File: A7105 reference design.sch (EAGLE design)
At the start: 38 parts, among them J1 JST-SH-3, SW1 BUTTON, U1 A7105, U2 ATTINY167, U3 NMOS, X1 ECX-2236

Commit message: Finished integrated rev 0.2
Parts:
- removed J1: JST-SH-3, nikdavis:JST-SH-3
- removed U$3, U$4: TESTPAD, AlienWhoop:TESTPAD
- added C19: 1uF, Perfect_0402:CAP_0402
- added U$10, U$11, U$12, U$6, U$7, U$8, U$9: TESTPAD, AlienWhoop:TESTPAD
- U3: value NMOS -> NMOSSOT833B/1006; device nikdavis:NMOS -> nikdavis:NMOSSOT833B/1006
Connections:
- new net GPIO1: U1.GIO1, U2.PA0
- net GND: now also C19.2, U$9.1; no longer J1.2, J1.P$1, U$4.1
- net MOSI: now also U$12.1
- net RESET: now also U$7.1
- net SBUS: now also U$6.1; no longer J1.3
- net SCK: now also U$10.1
- net SDIO: now also U$11.1
- net VCC: now also C19.1, U$8.1; no longer J1.1, U$3.1

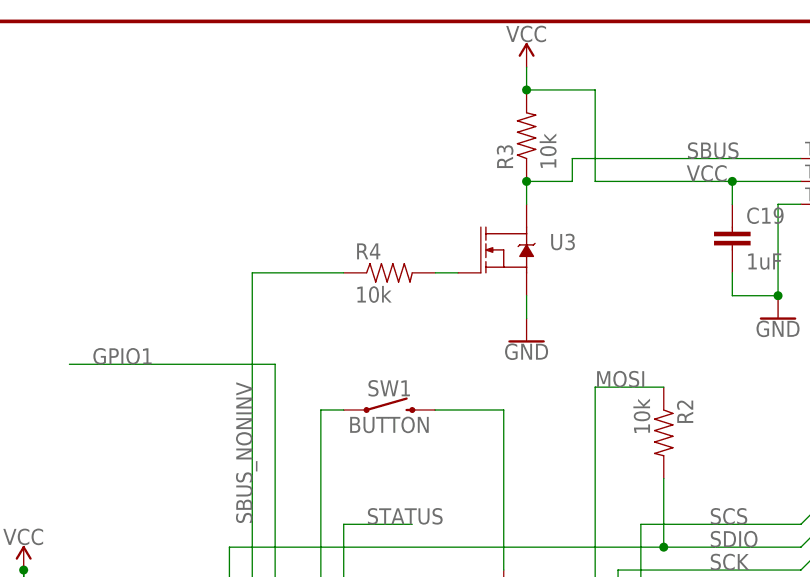
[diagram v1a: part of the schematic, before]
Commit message: Add bind pull up
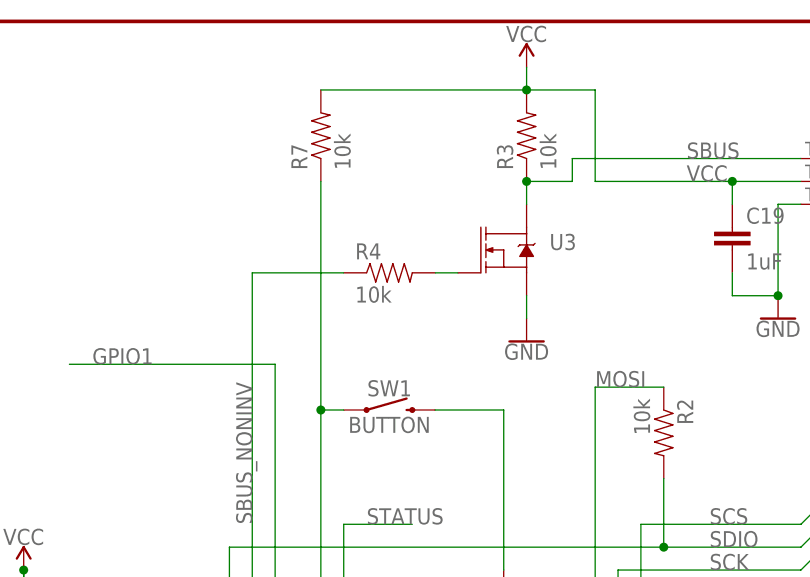
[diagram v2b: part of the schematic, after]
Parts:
- added R7: 10k, Perfect_0402:RES_0402
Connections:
- net BIND: now also R7.1
- net VCC: now also R7.2
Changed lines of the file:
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@@
 <part name="U$11" library="AlienWhoop" deviceset="TESTPAD" device=""/>
 <part name="U$12" library="AlienWhoop" deviceset="TESTPAD" device=""/>
+<part name="R7" library="Perfect_0402" deviceset="RES_0402" device="" value="10k"/>
 </parts>
 <sheets>
@@
 <instance part="U$11" gate="G$1" x="180.34" y="33.02" smashed="yes"/>
 <instance part="U$12" gate="G$1" x="180.34" y="30.48" smashed="yes"/>
+<instance part="R7" gate="G$1" x="109.22" y="119.38" smashed="yes" rot="R90">
+<attribute name="NAME" x="107.7214" y="120.65" size="1.778" layer="95" rot="R90"/>
+<attribute name="VALUE" x="112.522" y="120.65" size="1.778" layer="96" rot="R90"/>
+</instance>
 </instances>
 <busses>
@@
 <wire x1="154.94" y1="119.38" x2="154.94" y2="116.84" width="0.1524" layer="91"/>
 <junction x="154.94" y="119.38"/>
+<pinref part="R7" gate="G$1" pin="2"/>
+<wire x1="109.22" y1="129.54" x2="132.08" y2="129.54" width="0.1524" layer="91"/>
 </segment>
 <segment>
@@
 <wire x1="109.22" y1="93.98" x2="109.22" y2="73.66" width="0.1524" layer="91"/>
 <wire x1="109.22" y1="93.98" x2="111.76" y2="93.98" width="0.1524" layer="91"/>
-</segment>
-</net>
+<wire x1="109.22" y1="93.98" x2="109.22" y2="119.38" width="0.1524" layer="91"/>
+<junction x="109.22" y="93.98"/>
+<pinref part="R7" gate="G$1" pin="1"/>
+</segment>
+</net>

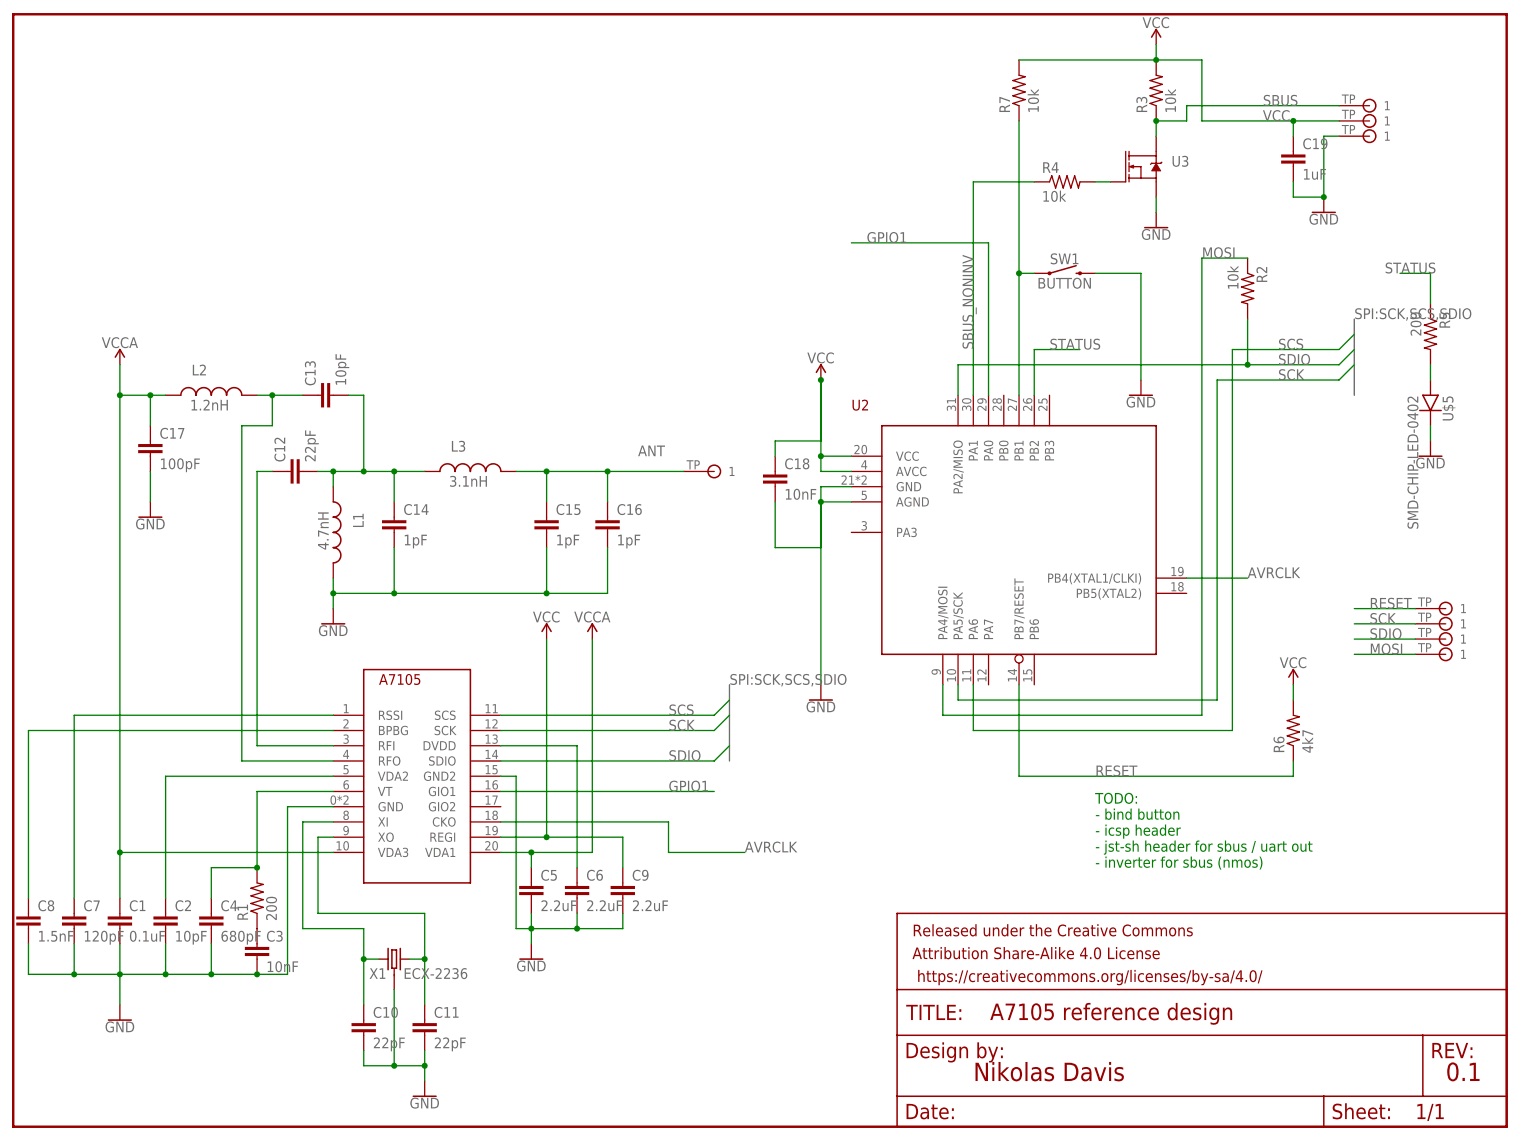
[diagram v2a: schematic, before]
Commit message: Start STM rehaul -- stuck on EEPROM decision
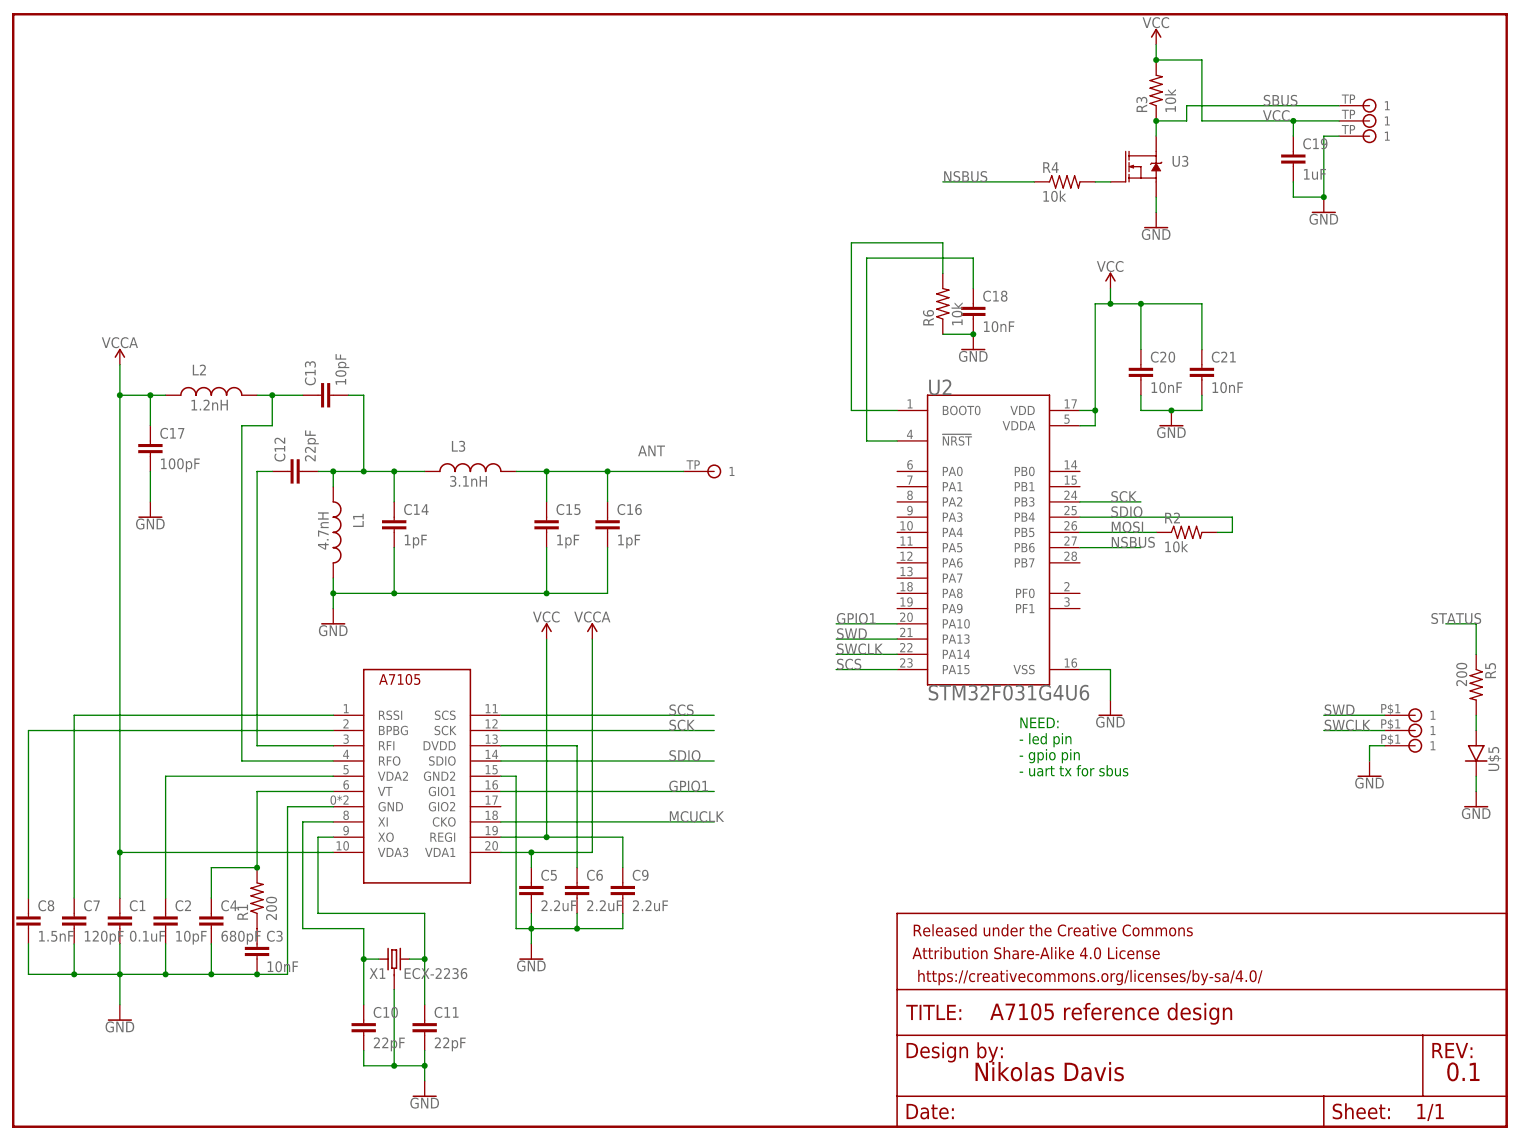
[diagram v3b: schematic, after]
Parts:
- removed R7: 10k, Perfect_0402:RES_0402
- removed SW1: BUTTON, nikdavis:BUTTON
- removed U$10, U$11, U$12, U$7: TESTPAD, AlienWhoop:TESTPAD
- added C20, C21: 10nF, Perfect_0402:CAP_0402
- added TP1, TP2, TP3: TESTPAD, nikdavis:TESTPAD
- R6: value 4k7 -> 10k
- U2: value ATTINY167 -> STM32F031G4U6; device nikdavis:ATTINY167 -> STM32F031G4U6:STM32F031G4U6
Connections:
- removed net AVRCLK: U1.CKO, U2.PB4(XTAL1/CLKI)
- removed net BIND: R7.1, SW1.1, U2.PB1
- removed net RESET: R6.1, U$7.1, U2.PB7/RESET
- removed net SBUS_NONINV: R4.1, U2.PA1
- new net MCUCLK: U1.CKO
- new net N$11: C18.1, U2.!NRST
- new net N$5: R6.2, U2.BOOT0
- new net NSBUS: R4.1, U2.PB6
- new net SWCLK: TP2.1, U2.PA14
- new net SWD: TP1.1, U2.PA13
- net GND: now also C20.2, C21.2, R6.1, TP3.1, U2.VSS; no longer SW1.2, U2.AGND, U2.GND
- net GPIO1: now also U2.PA10; no longer U2.PA0
- net MOSI: now also U2.PB5; no longer U$12.1, U2.PA4/MOSI
- net SCK: now also U2.PB3; no longer U$10.1, U2.PA5/SCK
- net SCS: now also U2.PA15; no longer U2.PA6
- net SDIO: now also U2.PB4; no longer U$11.1, U2.PA2/MISO
- net STATUS: no longer U2.PB2
- net VCC: now also C20.1, C21.1, U2.VDD, U2.VDDA; no longer C18.1, R6.2, R7.2, U2.AVCC, U2.VCC
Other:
- note added: "NEED: - led pin - gpio pin - uart tx for sbus"
- note removed: "TODO: - bind button - icsp header - jst-sh header for sbus / uart out - inverter for sbus (nmos)"
- moved on the sheet: C18, R2, R5, R6, U$5

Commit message: Small edits
Bit of board prep organization. Small schematic clean up and notes.
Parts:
- removed C21: 10nF, Perfect_0402:CAP_0402
- C20: value 10nF -> 0.1uF
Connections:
- net GND: no longer C21.2
- net VCC: no longer C21.1
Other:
- note added: "NEED: - led pin - gpio pin (pick one with edge interrupts close to a7105) - uart tx for sbus"
- note removed: "NEED: - led pin - gpio pin - uart tx for sbus"
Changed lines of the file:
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@@
 <part name="U2" library="STM32F031G4U6" deviceset="STM32F031G4U6" device=""/>
 <part name="GND8" library="SparkFun-PowerSymbols" deviceset="GND" device=""/>
-<part name="C20" library="Perfect_0402" deviceset="CAP_0402" device="" value="10nF"/>
+<part name="C20" library="Perfect_0402" deviceset="CAP_0402" device="" value="0.1uF"/>
 <part name="GND12" library="SparkFun-PowerSymbols" deviceset="GND" device=""/>
-<part name="C21" library="Perfect_0402" deviceset="CAP_0402" device="" value="10nF"/>
 <part name="GND13" library="SparkFun-PowerSymbols" deviceset="GND" device=""/>
 <part name="SUPPLY3" library="SparkFun-PowerSymbols" deviceset="VCC" device=""/>
@@
 <text x="101.6" y="-40.64" size="3.048" layer="94">Nikolas Davis</text>
 <text x="180.34" y="-40.64" size="3.048" layer="94">0.1</text>
-<text x="109.22" y="10.16" size="1.778" layer="91">NEED:
+<text x="88.9" y="5.08" size="1.778" layer="91">NEED:
 - led pin
-- gpio pin
+- gpio pin (pick one with edge interrupts close to a7105)
 - uart tx for sbus</text>
 </plain>
@@
 <attribute name="VALUE" x="101.6" y="81.026" size="1.778" layer="96" align="top-center"/>
 </instance>
-<instance part="C21" gate="G$1" x="139.7" y="73.66" smashed="yes">
-<attribute name="NAME" x="141.224" y="79.121" size="1.778" layer="95"/>
-<attribute name="VALUE" x="141.224" y="74.041" size="1.778" layer="96"/>
-</instance>
-<instance part="GND13" gate="1" x="134.62" y="68.58" smashed="yes">
-<attribute name="VALUE" x="134.62" y="68.326" size="1.778" layer="96" align="top-center"/>
+<instance part="GND13" gate="1" x="129.54" y="68.58" smashed="yes">
+<attribute name="VALUE" x="129.54" y="68.326" size="1.778" layer="96" align="top-center"/>
 </instance>
 <instance part="SUPPLY3" gate="G$1" x="124.46" y="91.44" smashed="yes">
@@
 <wire x1="129.54" y1="73.66" x2="129.54" y2="71.12" width="0.1524" layer="91"/>
 <pinref part="GND13" gate="1" pin="GND"/>
-<wire x1="129.54" y1="71.12" x2="134.62" y2="71.12" width="0.1524" layer="91"/>
-<pinref part="C21" gate="G$1" pin="2"/>
-<wire x1="139.7" y1="73.66" x2="139.7" y2="71.12" width="0.1524" layer="91"/>
-<wire x1="139.7" y1="71.12" x2="134.62" y2="71.12" width="0.1524" layer="91"/>
-<junction x="134.62" y="71.12"/>
 </segment>
 </net>
@@
 <wire x1="121.92" y1="68.58" x2="121.92" y2="71.12" width="0.1524" layer="91"/>
 <junction x="121.92" y="71.12"/>
-<wire x1="129.54" y1="88.9" x2="139.7" y2="88.9" width="0.1524" layer="91"/>
-<junction x="129.54" y="88.9"/>
-<pinref part="C21" gate="G$1" pin="1"/>
-<wire x1="139.7" y1="88.9" x2="139.7" y2="81.28" width="0.1524" layer="91"/>
-</segment>
-</net>
+</segment>
+</net>
